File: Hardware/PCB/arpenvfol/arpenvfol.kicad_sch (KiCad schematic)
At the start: 76 parts

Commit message: BOM
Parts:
- J1, J11, J12, J2, J4: SKU (none) -> A-1121; Vendor (none) -> Tayda
- MK1: SKU (none) -> A-5010; Vendor (none) -> Tayda
- RV1: SKU (none) -> A-1982
- RV2: SKU (none) -> A-1984
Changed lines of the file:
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@@
+      (effects (font (size 1.27 1.27)) hide)
+    )
+    (property "Description" "Resistor, 1/4 W metal film" (id 5) (at 219.71 49.53 0)
       (effects (font (size 1.27 1.27)) hide)
     )
@@
     )
     (property "Description" "1/4\" jack, vertical, TR" (id 4) (at 247.65 99.06 0)
+      (effects (font (size 1.27 1.27)) hide)
+    )
+    (property "SKU" "A-1121" (id 5) (at 247.65 99.06 0)
+      (effects (font (size 1.27 1.27)) hide)
+    )
+    (property "Vendor" "Tayda" (id 6) (at 247.65 99.06 0)
       (effects (font (size 1.27 1.27)) hide)
     )
@@
     )
     (property "Vendor" "Tayda" (id 4) (at 81.28 67.31 0)
+      (effects (font (size 1.27 1.27)) hide)
+    )
+    (property "Description" "Resistor, 1/4 W metal film" (id 5) (at 81.28 67.31 0)
       (effects (font (size 1.27 1.27)) hide)
     )
@@
       (effects (font (size 1.27 1.27)) hide)
     )
+    (property "Description" "Resistor, 1/4 W metal film" (id 5) (at 187.96 45.72 0)
+      (effects (font (size 1.27 1.27)) hide)
+    )
     (pin "1")
     (pin "2")
@@
       (effects (font (size 1.27 1.27)) hide)
     )
+    (property "SKU" "A-1121" (id 5) (at 243.84 43.18 0)
+      (effects (font (size 1.27 1.27)) hide)
+    )
+    (property "Vendor" "Tayda" (id 6) (at 243.84 43.18 0)
+      (effects (font (size 1.27 1.27)) hide)
+    )
     (pin "S")
     (pin "T")
@@
     )
     (property "Vendor" "Tayda" (id 4) (at 134.62 21.59 0)
+      (effects (font (size 1.27 1.27)) hide)
+    )
+    (property "Description" "Resistor, 1/4 W metal film" (id 5) (at 134.62 21.59 0)
       (effects (font (size 1.27 1.27)) hide)
     )
@@
       (effects (font (size 1.27 1.27)) hide)
     )
+    (property "Description" "Resistor, 1/4 W metal film" (id 5) (at 172.72 106.68 0)
+      (effects (font (size 1.27 1.27)) hide)
+    )
     (pin "1")
     (pin "2")
@@
     )
     (property "Description" "1/4\" jack, vertical, TR, switched" (id 4) (at 40.64 27.94 0)
+      (effects (font (size 1.27 1.27)) hide)
+    )
+    (property "SKU" "A-1121" (id 5) (at 40.64 27.94 0)
+      (effects (font (size 1.27 1.27)) hide)
+    )
+    (property "Vendor" "Tayda" (id 6) (at 40.64 27.94 0)
       (effects (font (size 1.27 1.27)) hide)
     )
@@
       (effects (font (size 1.27 1.27)) hide)
     )
+    (property "Description" "Resistor, 1/4 W metal film" (id 5) (at 149.86 45.72 0)
+      (effects (font (size 1.27 1.27)) hide)
+    )
     (pin "1")
     (pin "2")
@@
       (effects (font (size 1.27 1.27)) hide)
     )
+    (property "Description" "Resistor, 1/4 W metal film" (id 5) (at 86.36 21.59 0)
+      (effects (font (size 1.27 1.27)) hide)
+    )
     (pin "1")
     (pin "2")
@@
       (effects (font (size 1.27 1.27)) hide)
     )
+    (property "SKU" "A-1121" (id 5) (at 36.83 110.49 0)
+      (effects (font (size 1.27 1.27)) hide)
+    )
+    (property "Vendor" "Tayda" (id 6) (at 36.83 110.49 0)
+      (effects (font (size 1.27 1.27)) hide)
+    )
     (pin "S")
     (pin "T")
@@
     )
     (property "Vendor" "Tayda" (id 4) (at 219.71 105.41 0)
+      (effects (font (size 1.27 1.27)) hide)
+    )
+    (property "Description" "Resistor, 1/4 W metal film" (id 5) (at 219.71 105.41 0)
       (effects (font (size 1.27 1.27)) hide)
     )
@@
       (effects (font (size 1.27 1.27)) hide)
     )
+    (property "Description" "Linear potentiometer, panel mount" (id 5) (at 167.64 143.51 0)
+      (effects (font (size 1.27 1.27)) hide)
+    )
+    (property "SKU" "A-1982" (id 6) (at 167.64 143.51 0)
+      (effects (font (size 1.27 1.27)) hide)
+    )
     (pin "1")
     (pin "2")
@@
       (effects (font (size 1.27 1.27)) hide)
     )
+    (property "SKU" "A-5010" (id 4) (at 167.64 130.81 0)
+      (effects (font (size 1.27 1.27)) hide)
+    )
+    (property "Vendor" "Tayda" (id 5) (at 167.64 130.81 0)
+      (effects (font (size 1.27 1.27)) hide)
+    )
     (pin "1")
     (pin "2")
@@
       (effects (font (size 1.27 1.27)) hide)
     )
+    (property "Description" "Resistor, 1/4 W metal film" (id 5) (at 90.17 121.92 0)
+      (effects (font (size 1.27 1.27)) hide)
+    )
     (pin "1")
     (pin "2")
@@
       (effects (font (size 1.27 1.27)) hide)
     )
+    (property "Description" "Resistor, 1/4 W metal film" (id 5) (at 191.77 21.59 0)
+      (effects (font (size 1.27 1.27)) hide)
+    )
     (pin "1")
     (pin "2")
@@
     )
     (property "Vendor" "Tayda" (id 4) (at 76.2 53.34 0)
+      (effects (font (size 1.27 1.27)) hide)
+    )
+    (property "Description" "Resistor, 1/4 W metal film" (id 5) (at 76.2 53.34 0)
       (effects (font (size 1.27 1.27)) hide)
     )
@@
       (effects (font (size 1.27 1.27)) hide)
     )
+    (property "Description" "Resistor, 1/4 W metal film" (id 5) (at 59.69 27.94 0)
+      (effects (font (size 1.27 1.27)) hide)
+    )
     (pin "1")
     (pin "2")
@@
       (effects (font (size 1.27 1.27)) hide)
     )
+    (property "Description" "Resistor, 1/4 W metal film" (id 5) (at 80.01 99.06 0)
+      (effects (font (size 1.27 1.27)) hide)
+    )
     (pin "1")
     (pin "2")
@@
       (effects (font (size 1.27 1.27)) hide)
     )
+    (property "Description" "Resistor, 1/4 W metal film" (id 5) (at 116.84 43.18 0)
+      (effects (font (size 1.27 1.27)) hide)
+    )
     (pin "1")
     (pin "2")
@@
     )
     (property "Vendor" "Tayda" (id 4) (at 99.06 116.84 0)
+      (effects (font (size 1.27 1.27)) hide)
+    )
+    (property "Description" "Resistor, 1/4 W metal film" (id 5) (at 99.06 116.84 0)
       (effects (font (size 1.27 1.27)) hide)
     )
@@
       (effects (font (size 1.27 1.27)) hide)
     )
+    (property "Description" "Resistor, 1/4 W metal film" (id 5) (at 227.33 99.06 0)
+      (effects (font (size 1.27 1.27)) hide)
+    )
     (pin "1")
     (pin "2")
@@
       (effects (font (size 1.27 1.27)) hide)
     )
+    (property "Description" "Resistor, 1/4 W metal film" (id 5) (at 175.26 45.72 0)
+      (effects (font (size 1.27 1.27)) hide)
+    )
     (pin "1")
     (pin "2")
@@
       (effects (font (size 1.27 1.27)) hide)
     )
+    (property "Description" "Resistor, 1/4 W metal film" (id 5) (at 224.79 43.18 0)
+      (effects (font (size 1.27 1.27)) hide)
+    )
     (pin "1")
     (pin "2")
@@
       (effects (font (size 1.27 1.27)) hide)
     )
+    (property "Description" "Resistor, 1/4 W metal film" (id 5) (at 59.69 129.54 0)
+      (effects (font (size 1.27 1.27)) hide)
+    )
     (pin "1")
     (pin "2")
@@
       (effects (font (size 1.27 1.27)) hide)
     )
+    (property "Description" "Resistor, 1/4 W metal film" (id 5) (at 80.01 129.54 0)
+      (effects (font (size 1.27 1.27)) hide)
+    )
     (pin "1")
     (pin "2")
@@
     )
     (property "Vendor" "Tayda" (id 4) (at 87.63 72.39 0)
+      (effects (font (size 1.27 1.27)) hide)
+    )
+    (property "Description" "Resistor, 1/4 W metal film" (id 5) (at 87.63 72.39 0)
       (effects (font (size 1.27 1.27)) hide)
     )
@@
       (effects (font (size 1.27 1.27)) hide)
     )
+    (property "Description" "Resistor, 1/4 W metal film" (id 5) (at 58.42 99.06 0)
+      (effects (font (size 1.27 1.27)) hide)
+    )
     (pin "1")
     (pin "2")
@@
       (effects (font (size 1.27 1.27)) hide)
     )
+    (property "Description" "Resistor, 1/4 W metal film" (id 5) (at 162.56 45.72 0)
+      (effects (font (size 1.27 1.27)) hide)
+    )
     (pin "1")
     (pin "2")
@@
     )
     (property "Description" "1/4\" jack, vertical, TR, switched" (id 4) (at 156.21 101.6 0)
+      (effects (font (size 1.27 1.27)) hide)
+    )
+    (property "SKU" "A-1121" (id 5) (at 156.21 101.6 0)
+      (effects (font (size 1.27 1.27)) hide)
+    )
+    (property "Vendor" "Tayda" (id 6) (at 156.21 101.6 0)
       (effects (font (size 1.27 1.27)) hide)
     )
@@
     )
     (property "Vendor" "Tayda" (id 4) (at 116.84 52.07 0)
+      (effects (font (size 1.27 1.27)) hide)
+    )
+    (property "Description" "Resistor, 1/4 W metal film" (id 5) (at 116.84 52.07 0)
       (effects (font (size 1.27 1.27)) hide)
     )
@@
       (effects (font (size 1.27 1.27)) hide)
     )
+    (property "Description" "Resistor, 1/4 W metal film" (id 5) (at 99.06 129.54 0)
+      (effects (font (size 1.27 1.27)) hide)
+    )
     (pin "1")
     (pin "2")
@@
       (effects (font (size 1.27 1.27)) hide)
     )
+    (property "Description" "Resistor, 1/4 W metal film" (id 5) (at 193.04 86.36 0)
+      (effects (font (size 1.27 1.27)) hide)
+    )
     (pin "1")
     (pin "2")
@@
     )
     (property "Vendor" "Tayda" (id 4) (at 184.15 106.68 0)
+      (effects (font (size 1.27 1.27)) hide)
+    )
+    (property "Description" "Resistor, 1/4 W metal film" (id 5) (at 184.15 106.68 0)
       (effects (font (size 1.27 1.27)) hide)
     )
@@
       (effects (font (size 1.27 1.27)) hide)
     )
+    (property "Description" "Linear potentiometer, panel mount" (id 5) (at 167.64 156.21 0)
+      (effects (font (size 1.27 1.27)) hide)
+    )
+    (property "SKU" "A-1984" (id 6) (at 167.64 156.21 0)
+      (effects (font (size 1.27 1.27)) hide)
+    )
     (pin "1")
     (pin "2")
@@
       (effects (font (size 1.27 1.27)) hide)
     )
+    (property "Description" "Resistor, 1/4 W metal film" (id 5) (at 208.28 21.59 0)
+      (effects (font (size 1.27 1.27)) hide)
+    )

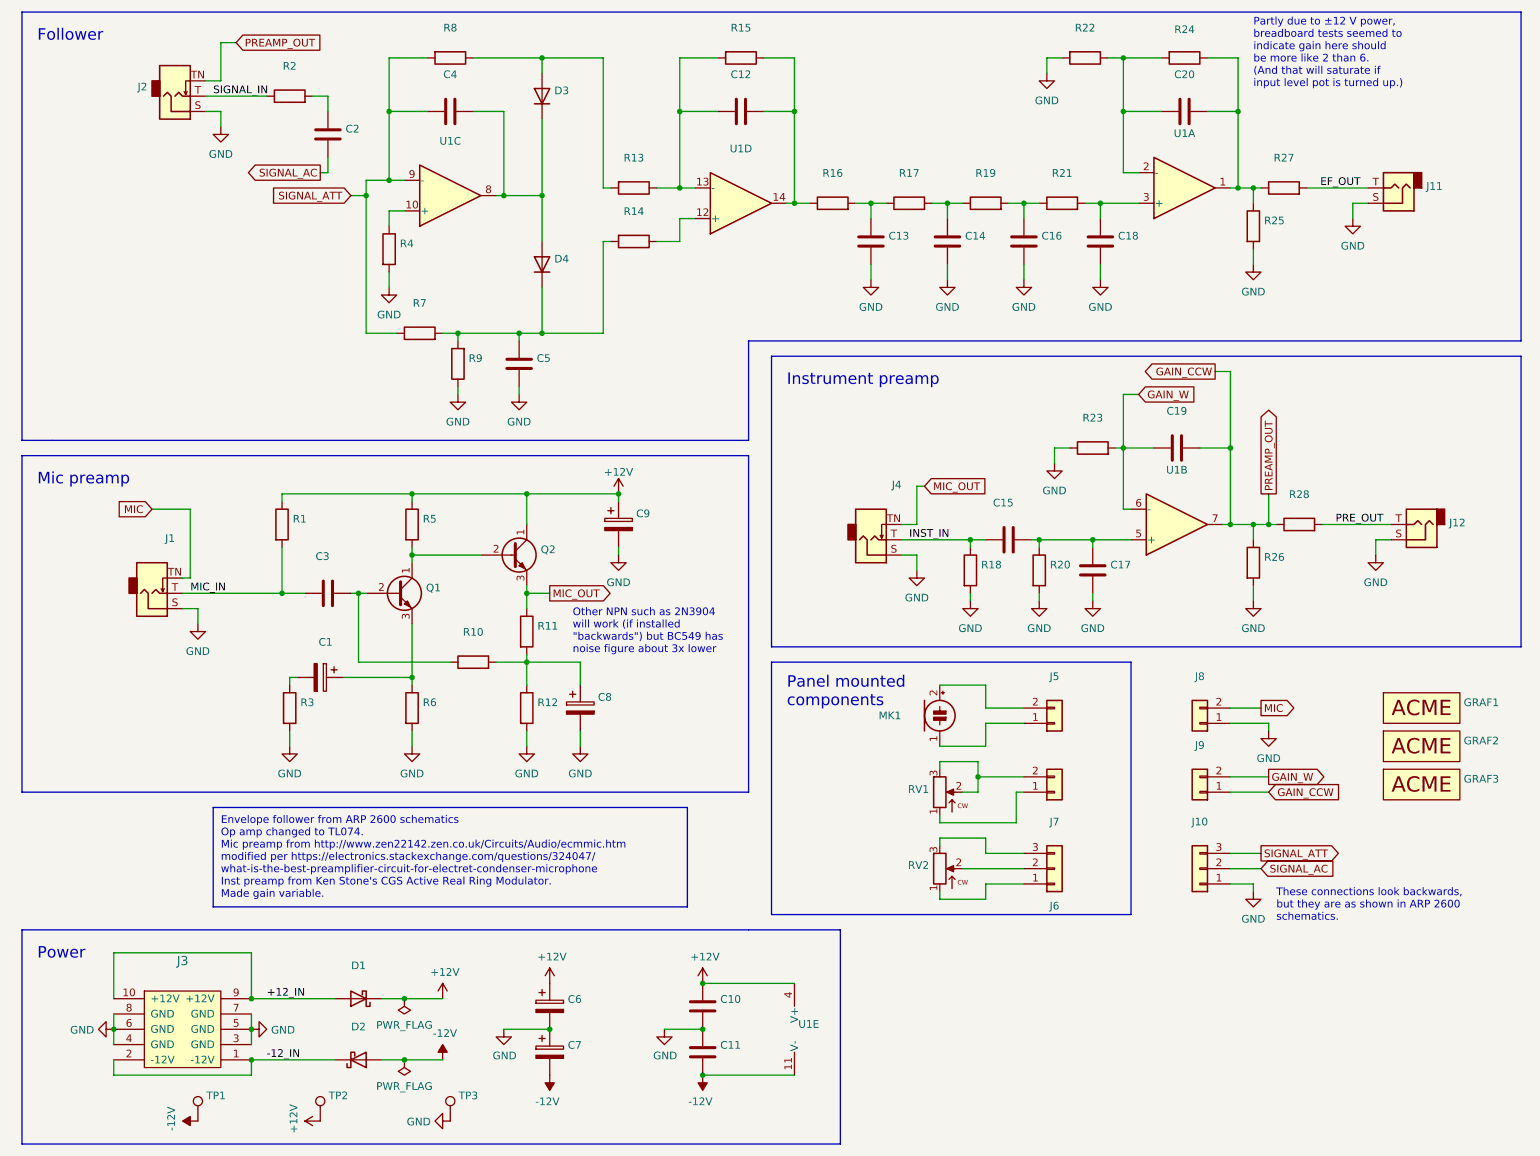
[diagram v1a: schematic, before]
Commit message: Change 2 resistor values
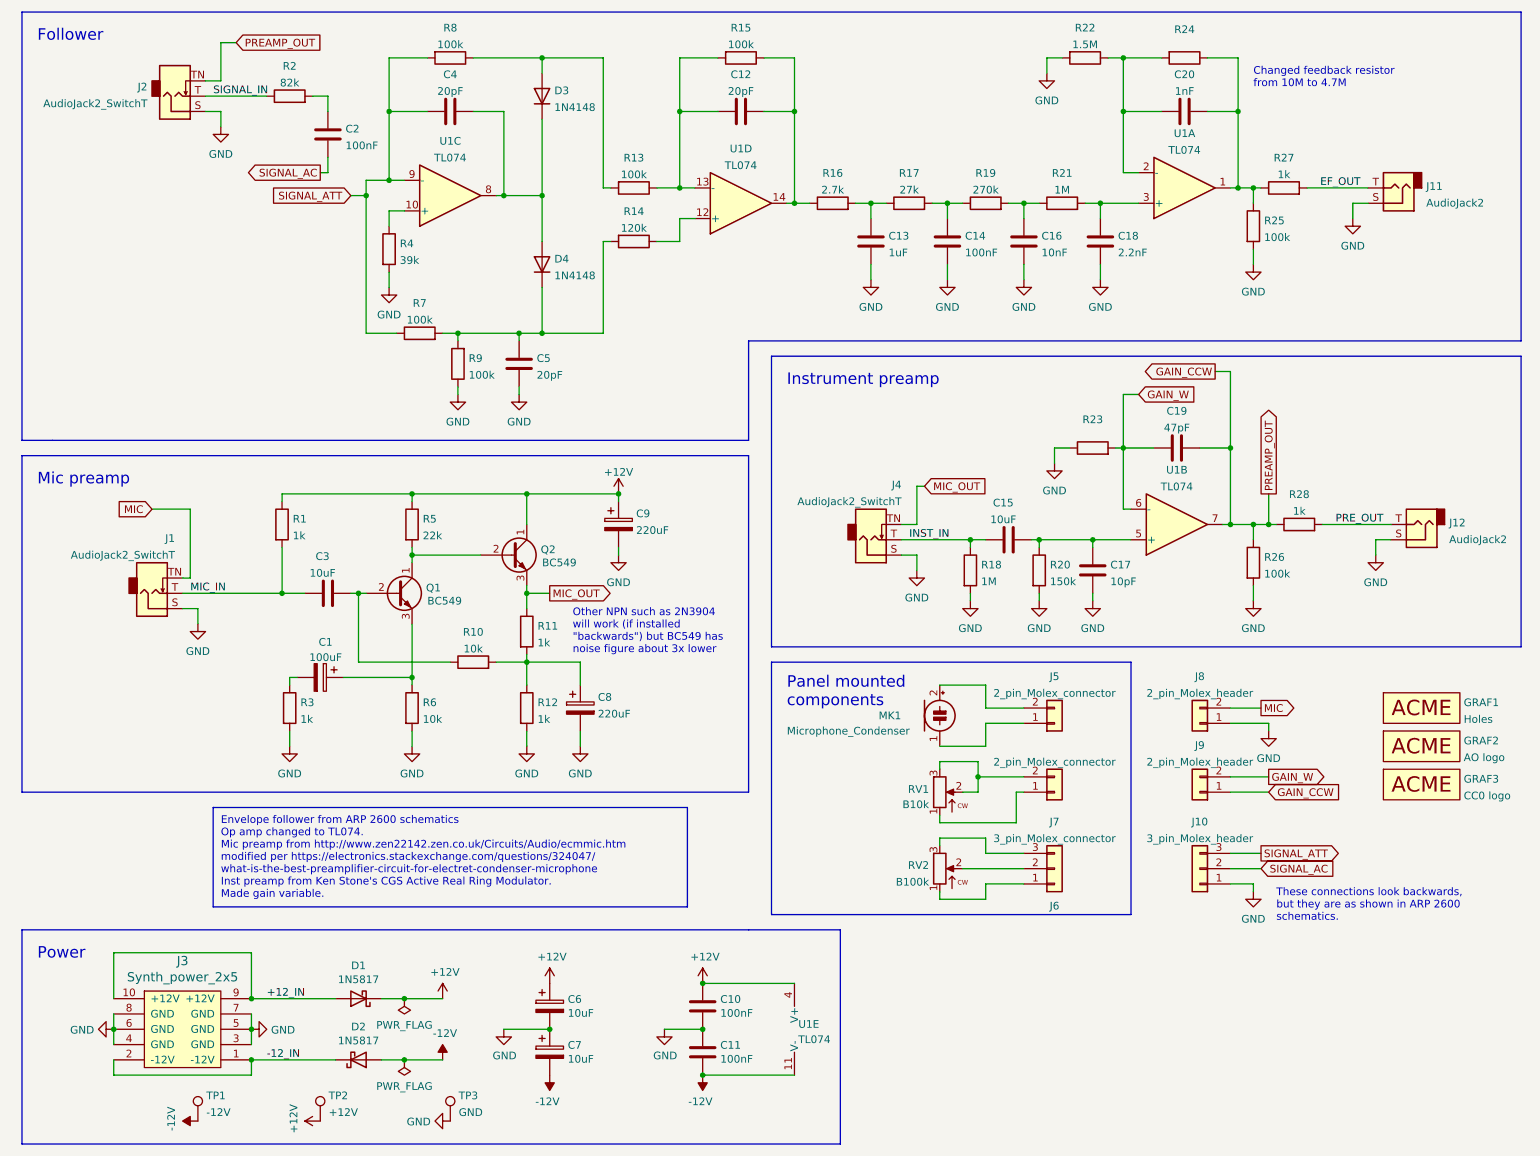
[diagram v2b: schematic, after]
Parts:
- C1: value (none) -> 100uF; footprint (none) -> ao_tht:CP_Radial_D6.3mm_P2.50mm
- C10, C11: value (none) -> 100nF; footprint (none) -> ao_tht:C_Disc_D3.0mm_W1.6mm_P2.50mm
- C12, C4, C5: value (none) -> 20pF; footprint (none) -> ao_tht:C_Disc_D5.0mm_W2.5mm_P5.00mm
- C13: value (none) -> 1uF; footprint (none) -> ao_tht:C_Rect_L7.2mm_W7.2mm_P5.00mm_FKS2_FKP2_MKS2_MKP2
- C14, C2: value (none) -> 100nF; footprint (none) -> ao_tht:C_Rect_L7.2mm_W2.5mm_P5.00mm_FKS2_FKP2_MKS2_MKP2
- C15, C3: value (none) -> 10uF; footprint (none) -> ao_tht:C_Radial_D8.0mm_H11.5mm_P3.50mm
- C16: value (none) -> 10nF; footprint (none) -> ao_tht:C_Rect_L7.2mm_W2.5mm_P5.00mm_FKS2_FKP2_MKS2_MKP2
- C17: value (none) -> 10pF; footprint (none) -> ao_tht:C_Disc_D5.0mm_W2.5mm_P5.00mm
- C18: value (none) -> 2.2nF; footprint (none) -> ao_tht:C_Rect_L7.2mm_W2.5mm_P5.00mm_FKS2_FKP2_MKS2_MKP2
- C19: value (none) -> 47pF; footprint (none) -> ao_tht:C_Disc_D5.0mm_W2.5mm_P5.00mm
- C20: value (none) -> 1nF; footprint (none) -> ao_tht:C_Rect_L7.2mm_W2.5mm_P5.00mm_FKS2_FKP2_MKS2_MKP2
- C6, C7: value (none) -> 10uF; footprint (none) -> ao_tht:CP_Radial_D6.3mm_P2.50mm
- C8, C9: value (none) -> 220uF; footprint (none) -> ao_tht:CP_Radial_D6.3mm_P2.50mm
- D1, D2: value (none) -> 1N5817; footprint (none) -> ao_tht:D_DO-41_SOD81_P10.16mm_Horizontal
- D3, D4: value (none) -> 1N4148; footprint (none) -> ao_tht:D_DO-35_SOD27_P7.62mm_Horizontal
- GRAF1: value (none) -> Holes; footprint (none) -> arpenvfol:arpenvfol_panel_holes
- GRAF2: value (none) -> AO logo; footprint (none) -> ao_tht:analogoutput_12mm
- GRAF3: value (none) -> CC0 logo; footprint (none) -> ao_tht:CC0_logo
- J1, J2, J4: value (none) -> AudioJack2_SwitchT; footprint (none) -> ao_tht:Jack_6.35mm_PJ_629HAN_slots
- J10: value (none) -> 3_pin_Molex_header; footprint (none) -> ao_tht:Molex_KK-254_AE-6410-03A_1x03_P2.54mm_Vertical
- J11, J12: value (none) -> AudioJack2; footprint (none) -> ao_tht:Jack_6.35mm_PJ_629HAN_slots
- J3: value (none) -> Synth_power_2x5; footprint (none) -> ao_tht:Power_Header
- J5, J6: value (none) -> 2_pin_Molex_connector; footprint (none) -> ao_tht:Molex_KK-254_AE-6410-02A_1x02_P2.54mm_Vertical
- J7: value (none) -> 3_pin_Molex_connector; footprint (none) -> ao_tht:Molex_KK-254_AE-6410-03A_1x03_P2.54mm_Vertical
- J8, J9: value (none) -> 2_pin_Molex_header; footprint (none) -> ao_tht:Molex_KK-254_AE-6410-02A_1x02_P2.54mm_Vertical
- MK1: value (none) -> Microphone_Condenser
- Q1, Q2: value (none) -> BC549; footprint (none) -> ao_tht:TO-92_Inline_Wide
- R1, R11, R12, R27, R28, R3: value (none) -> 1k; footprint (none) -> ao_tht:R_Axial_DIN0207_L6.3mm_D2.5mm_P10.16mm_Horizontal
- R10, R6: value (none) -> 10k; footprint (none) -> ao_tht:R_Axial_DIN0207_L6.3mm_D2.5mm_P10.16mm_Horizontal
- R13, R15, R25, R26, R7, R8, R9: value (none) -> 100k; footprint (none) -> ao_tht:R_Axial_DIN0207_L6.3mm_D2.5mm_P10.16mm_Horizontal
- R14: value (none) -> 120k; footprint (none) -> ao_tht:R_Axial_DIN0207_L6.3mm_D2.5mm_P10.16mm_Horizontal
- R16: value (none) -> 2.7k; footprint (none) -> ao_tht:R_Axial_DIN0207_L6.3mm_D2.5mm_P10.16mm_Horizontal
- R17: value (none) -> 27k; footprint (none) -> ao_tht:R_Axial_DIN0207_L6.3mm_D2.5mm_P10.16mm_Horizontal
- R18, R21: value (none) -> 1M; footprint (none) -> ao_tht:R_Axial_DIN0207_L6.3mm_D2.5mm_P10.16mm_Horizontal
- R19: value (none) -> 270k; footprint (none) -> ao_tht:R_Axial_DIN0207_L6.3mm_D2.5mm_P10.16mm_Horizontal
- R2: value (none) -> 82k; footprint (none) -> ao_tht:R_Axial_DIN0207_L6.3mm_D2.5mm_P10.16mm_Horizontal
- R20: value (none) -> 150k; footprint (none) -> ao_tht:R_Axial_DIN0207_L6.3mm_D2.5mm_P10.16mm_Horizontal
- R22: value (none) -> 1.5M; footprint (none) -> ao_tht:R_Axial_DIN0207_L6.3mm_D2.5mm_P10.16mm_Horizontal
- R23, R24: footprint (none) -> ao_tht:R_Axial_DIN0207_L6.3mm_D2.5mm_P10.16mm_Horizontal
- R4: value (none) -> 39k; footprint (none) -> ao_tht:R_Axial_DIN0207_L6.3mm_D2.5mm_P10.16mm_Horizontal
- R5: value (none) -> 22k; footprint (none) -> ao_tht:R_Axial_DIN0207_L6.3mm_D2.5mm_P10.16mm_Horizontal
- RV1: value (none) -> B10k
- RV2: value (none) -> B100k
- TP1: value (none) -> -12V; footprint (none) -> ao_tht:TestPoint_THTPad_D1.5mm_Drill0.7mm
- TP2: value (none) -> +12V; footprint (none) -> ao_tht:TestPoint_THTPad_D1.5mm_Drill0.7mm
- TP3: value (none) -> GND; footprint (none) -> ao_tht:TestPoint_THTPad_1.5x1.5mm_Drill0.7mm
- U1: value (none) -> TL074; footprint (none) -> ao_tht:DIP-14_W7.62mm_Socket_LongPads
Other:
- note added: "Changed feedback resistor from 10M to 4.7M"
- note removed: "Partly due to ±12 V power, breadboard tests seemed to indicate gain here should be more like 2 than 6. (And that will saturate if input level pot is turned up.)"
